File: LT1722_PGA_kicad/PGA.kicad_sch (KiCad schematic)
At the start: 8 parts, among them U4 LT1722

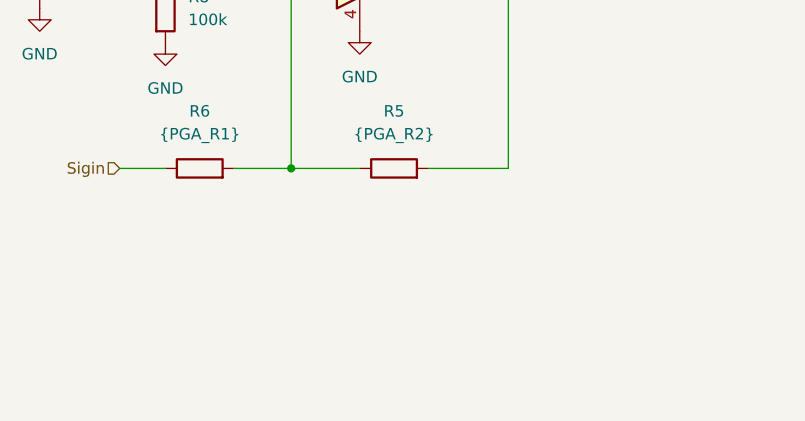
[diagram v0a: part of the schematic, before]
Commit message: change stage1 and pga to be tuned
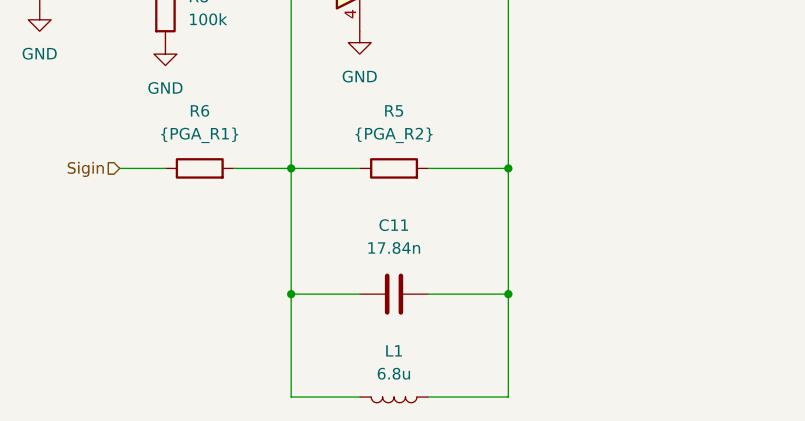
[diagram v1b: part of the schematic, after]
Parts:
- added C11: 17.84n, symbol Device:C
- added L1: 6.8u, symbol Device:L
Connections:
- net Sigout: now also C11.2, L1.1
- net at R5.1, R6.2, U4.2 (-): now also C11.1, L1.2
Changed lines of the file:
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@@
+	)
+	(junction
+		(at 114.3 109.22)
+		(diameter 0)
+		(color 0 0 0 0)
 	)
 	(junction
@@
 	)
 	(junction
+		(at 114.3 123.19)
+		(diameter 0)
+		(color 0 0 0 0)
+	)
+	(junction
 		(at 113.03 62.23)
 		(diameter 0)
@@
 		(color 0 0 0 0)
 	)
+	(junction
+		(at 90.17 123.19)
+		(diameter 0)
+		(color 0 0 0 0)
+	)
 	(wire
 		(pts
@@
 	(wire
 		(pts
+			(xy 90.17 109.22) (xy 90.17 123.19)
+		)
+		(stroke
+			(width 0)
+			(type default)
+		)
+	)
+	(wire
+		(pts
 			(xy 105.41 109.22) (xy 114.3 109.22)
 		)
@@
 	(wire
 		(pts
+			(xy 90.17 134.62) (xy 90.17 123.19)
+		)
+		(stroke
+			(width 0)
+			(type default)
+		)
+	)
+	(wire
+		(pts
 			(xy 90.17 88.9) (xy 90.17 109.22)
 		)
@@
 	(wire
 		(pts
+			(xy 97.79 134.62) (xy 90.17 134.62)
+		)
+		(stroke
+			(width 0)
+			(type default)
+		)
+	)
+	(wire
+		(pts
+			(xy 105.41 123.19) (xy 114.3 123.19)
+		)
+		(stroke
+			(width 0)
+			(type default)
+		)
+	)
+	(wire
+		(pts
 			(xy 114.3 86.36) (xy 114.3 109.22)
 		)
@@
 	(wire
 		(pts
+			(xy 105.41 134.62) (xy 114.3 134.62)
+		)
+		(stroke
+			(width 0)
+			(type default)
+		)
+	)
+	(wire
+		(pts
+			(xy 114.3 134.62) (xy 114.3 123.19)
+		)
+		(stroke
+			(width 0)
+			(type default)
+		)
+	)
+	(wire
+		(pts
 			(xy 101.6 54.61) (xy 113.03 54.61)
 		)
@@
 	(wire
 		(pts
+			(xy 114.3 109.22) (xy 114.3 123.19)
+		)
+		(stroke
+			(width 0)
+			(type default)
+		)
+	)
+	(wire
+		(pts
 			(xy 97.79 77.47) (xy 97.79 78.74)
 		)
@@
 		(pts
 			(xy 76.2 83.82) (xy 76.2 87.63)
+		)
+		(stroke
+			(width 0)
+			(type default)
+		)
+	)
+	(wire
+		(pts
+			(xy 97.79 123.19) (xy 90.17 123.19)
 		)
 		(stroke
@@
 	)
 	(symbol
+		(lib_id "Device:L")
+		(at 101.6 134.62 270)
+		(unit 1)
+		(exclude_from_sim no)
+		(in_bom yes)
+		(on_board yes)
+		(dnp no)
+		(fields_autoplaced yes)
+		(property "Reference" "L1"
+			(at 101.6 129.54 90)
+			(effects
+				(font
+					(size 1.27 1.27)
+				)
+			)
+		)
+		(property "Value" "6.8u"
+			(at 101.6 132.08 90)
+			(effects
+				(font
+					(size 1.27 1.27)
+				)
+			)
+		)
+		(property "Footprint" ""
+			(at 101.6 134.62 0)
+			(effects
+				(font
+					(size 1.27 1.27)
+				)
+				(hide yes)
+			)
+		)
+		(property "Datasheet" "~"
+			(at 101.6 134.62 0)
+			(effects
+				(font
+					(size 1.27 1.27)
+				)
+				(hide yes)
+			)
+		)
+		(property "Description" "Inductor"
+			(at 101.6 134.62 0)
+			(effects
+				(font
+					(size 1.27 1.27)
+				)
+				(hide yes)
+			)
+		)
+		(pin "2"
+		)
+		(pin "1"
+		)
+		(instances
+			(project "LT1722_PGA_kicad"
+				(path "/e9dc583c-35fc-43e6-96d7-d148e3dd184c/acfb5c68-7b0f-46bf-93eb-352c24d2de73"
+					(reference "L1")
+					(unit 1)
+				)
+			)
+		)
+	)
+	(symbol
 		(lib_id "Device:R")
 		(at 76.2 91.44 0)
@@
 					(unit 1)
 				)
+			)
+		)
+	)
+	(symbol
+		(lib_id "Device:C")
+		(at 101.6 123.19 90)
+		(unit 1)
+		(exclude_from_sim no)
+		(in_bom yes)
+		(on_board yes)
+		(dnp no)
+		(fields_autoplaced yes)
+		(property "Reference" "C11"
+			(at 101.6 115.57 90)
+			(effects
+				(font
+					(size 1.27 1.27)
+				)
+			)
+		)
+		(property "Value" "17.84n"
+			(at 101.6 118.11 90)
+			(effects
+				(font
+					(size 1.27 1.27)
+				)
+			)
+		)
+		(property "Footprint" ""
+			(at 105.41 122.2248 0)
+			(effects
+				(font
+					(size 1.27 1.27)
+				)
+				(hide yes)
+			)
+		)
+		(property "Datasheet" "~"
+			(at 101.6 123.19 0)
+			(effects
+				(font
+					(size 1.27 1.27)
+				)
+				(hide yes)
+			)
+		)
+		(property "Description" "Unpolarized capacitor"
+			(at 101.6 123.19 0)
+			(effects
+				(font
+					(size 1.27 1.27)
+				)
+				(hide yes)
+			)
+		)
+		(pin "2"
+		)
+		(pin "1"
+		)
+		(instances
+			(project "LT1722_PGA_kicad"
+				(path "/e9dc583c-35fc-43e6-96d7-d148e3dd184c/acfb5c68-7b0f-46bf-93eb-352c24d2de73"
+					(reference "C11")
+					(unit 1)
+				)

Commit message: add all changes
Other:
- moved on the sheet: C11, L1
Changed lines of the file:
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@@
+	)
+	(junction
+		(at 101.6 54.61)
+		(diameter 0)
+		(color 0 0 0 0)
+	)
+	(junction
+		(at 90.17 109.22)
+		(diameter 0)
+		(color 0 0 0 0)
+	)
+	(junction
+		(at 114.3 132.08)
+		(diameter 0)
+		(color 0 0 0 0)
+	)
+	(junction
+		(at 113.03 62.23)
+		(diameter 0)
+		(color 0 0 0 0)
+	)
+	(junction
+		(at 76.2 83.82)
+		(diameter 0)
+		(color 0 0 0 0)
 	)
 	(junction
@@
 	)
 	(junction
-		(at 101.6 54.61)
+		(at 90.17 132.08)
 		(diameter 0)
 		(color 0 0 0 0)
 	)
-	(junction
-		(at 90.17 109.22)
-		(diameter 0)
-		(color 0 0 0 0)
-	)
-	(junction
-		(at 114.3 123.19)
-		(diameter 0)
-		(color 0 0 0 0)
-	)
-	(junction
-		(at 113.03 62.23)
-		(diameter 0)
-		(color 0 0 0 0)
-	)
-	(junction
-		(at 76.2 83.82)
-		(diameter 0)
-		(color 0 0 0 0)
-	)
-	(junction
-		(at 90.17 123.19)
-		(diameter 0)
-		(color 0 0 0 0)
-	)
 	(wire
 		(pts
@@
 	(wire
 		(pts
-			(xy 90.17 109.22) (xy 90.17 123.19)
+			(xy 90.17 109.22) (xy 90.17 132.08)
 		)
 		(stroke
@@
 	(wire
 		(pts
-			(xy 90.17 134.62) (xy 90.17 123.19)
+			(xy 90.17 143.51) (xy 90.17 132.08)
 		)
 		(stroke
@@
 	(wire
 		(pts
-			(xy 97.79 134.62) (xy 90.17 134.62)
-		)
-		(stroke
-			(width 0)
-			(type default)
-		)
-	)
-	(wire
-		(pts
-			(xy 105.41 123.19) (xy 114.3 123.19)
+			(xy 97.79 143.51) (xy 90.17 143.51)
+		)
+		(stroke
+			(width 0)
+			(type default)
+		)
+	)
+	(wire
+		(pts
+			(xy 105.41 132.08) (xy 114.3 132.08)
 		)
 		(stroke
@@
 	(wire
 		(pts
+			(xy 114.3 109.22) (xy 114.3 132.08)
+		)
+		(stroke
+			(width 0)
+			(type default)
+		)
+	)
+	(wire
+		(pts
 			(xy 101.6 62.23) (xy 113.03 62.23)
 		)
@@
 	(wire
 		(pts
-			(xy 105.41 134.62) (xy 114.3 134.62)
-		)
-		(stroke
-			(width 0)
-			(type default)
-		)
-	)
-	(wire
-		(pts
-			(xy 114.3 134.62) (xy 114.3 123.19)
+			(xy 105.41 143.51) (xy 114.3 143.51)
+		)
+		(stroke
+			(width 0)
+			(type default)
+		)
+	)
+	(wire
+		(pts
+			(xy 114.3 143.51) (xy 114.3 132.08)
 		)
 		(stroke
@@
 	(wire
 		(pts
-			(xy 114.3 109.22) (xy 114.3 123.19)
-		)
-		(stroke
-			(width 0)
-			(type default)
-		)
-	)
-	(wire
-		(pts
 			(xy 97.79 77.47) (xy 97.79 78.74)
 		)
@@
 	(wire
 		(pts
-			(xy 97.79 123.19) (xy 90.17 123.19)
+			(xy 97.79 132.08) (xy 90.17 132.08)
 		)
 		(stroke
@@
 	(symbol
 		(lib_id "Device:L")
-		(at 101.6 134.62 270)
+		(at 101.6 143.51 270)
 		(unit 1)
 		(exclude_from_sim no)
@@
 		(fields_autoplaced yes)
 		(property "Reference" "L1"
-			(at 101.6 129.54 90)
+			(at 101.6 138.43 90)
 			(effects
 				(font
@@
 		)
 		(property "Value" "6.8u"
-			(at 101.6 132.08 90)
-			(effects
-				(font
-					(size 1.27 1.27)
-				)
-			)
-		)
-		(property "Footprint" ""
-			(at 101.6 134.62 0)
+			(at 101.6 140.97 90)
+			(effects
+				(font
+					(size 1.27 1.27)
+				)
+			)
+		)
+		(property "Footprint" ""
+			(at 101.6 143.51 0)
 			(effects
 				(font
@@
 		)
 		(property "Datasheet" "~"
-			(at 101.6 134.62 0)
+			(at 101.6 143.51 0)
 			(effects
 				(font
@@
 		)
 		(property "Description" "Inductor"
-			(at 101.6 134.62 0)
+			(at 101.6 143.51 0)
 			(effects
 				(font
@@
 	(symbol
 		(lib_id "Device:C")
-		(at 101.6 123.19 90)
+		(at 101.6 132.08 90)
 		(unit 1)
 		(exclude_from_sim no)
@@
 		(fields_autoplaced yes)
 		(property "Reference" "C11"
-			(at 101.6 115.57 90)
+			(at 101.6 124.46 90)
 			(effects
 				(font
@@
 		)
 		(property "Value" "17.84n"
-			(at 101.6 118.11 90)
-			(effects
-				(font
-					(size 1.27 1.27)
-				)
-			)
-		)
-		(property "Footprint" ""
-			(at 105.41 122.2248 0)
+			(at 101.6 127 90)
+			(effects
+				(font
+					(size 1.27 1.27)
+				)
+			)
+		)
+		(property "Footprint" ""
+			(at 105.41 131.1148 0)
 			(effects
 				(font
@@
 		)
 		(property "Datasheet" "~"
-			(at 101.6 123.19 0)
+			(at 101.6 132.08 0)
 			(effects
 				(font
@@
 		)
 		(property "Description" "Unpolarized capacitor"
-			(at 101.6 123.19 0)
-			(effects
-				(font
+			(at 101.6 132.08 0)
+			(effects
+				(font
